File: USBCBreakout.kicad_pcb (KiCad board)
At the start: 2 copper layers, 38 x 36 mm, 8 parts, among them J1 Conn_01x04, U1 PRTR5V0U2X-ai03-locallib

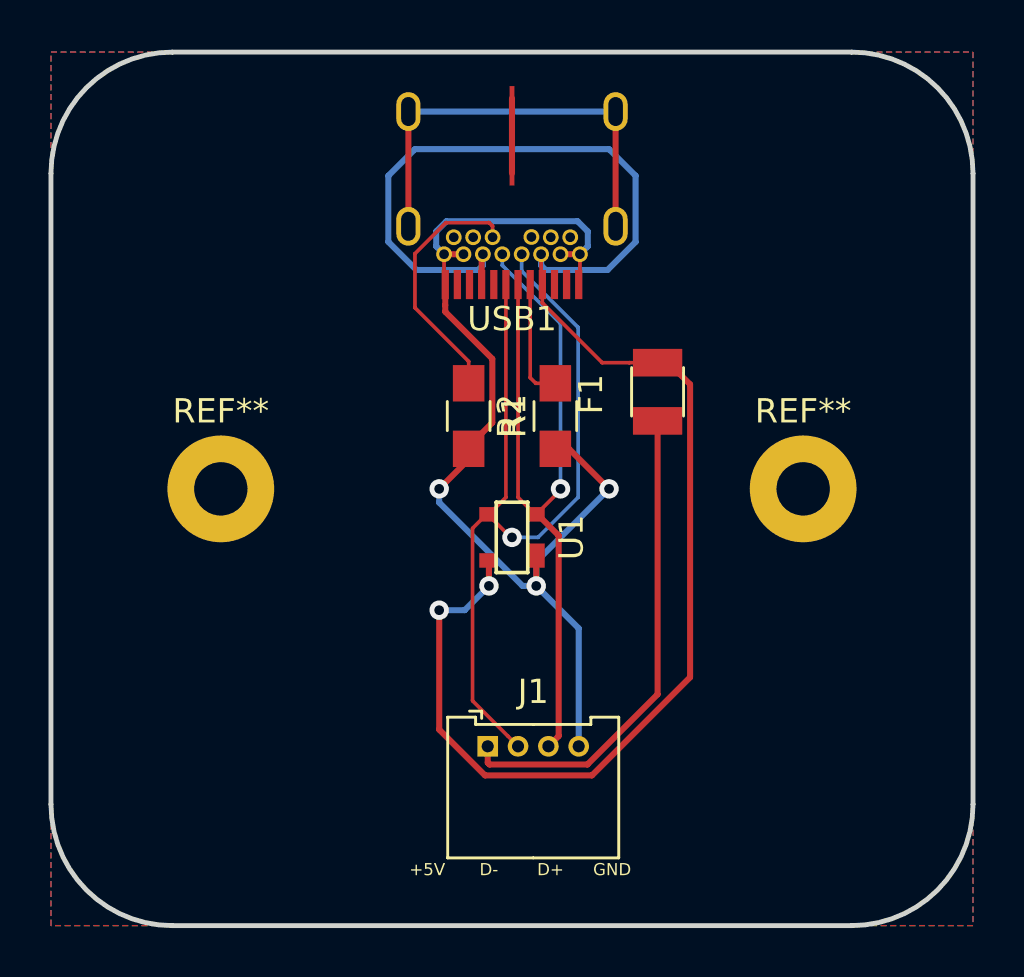
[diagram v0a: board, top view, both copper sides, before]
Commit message: Made breakout slimmer, should accomodate much better panelling.
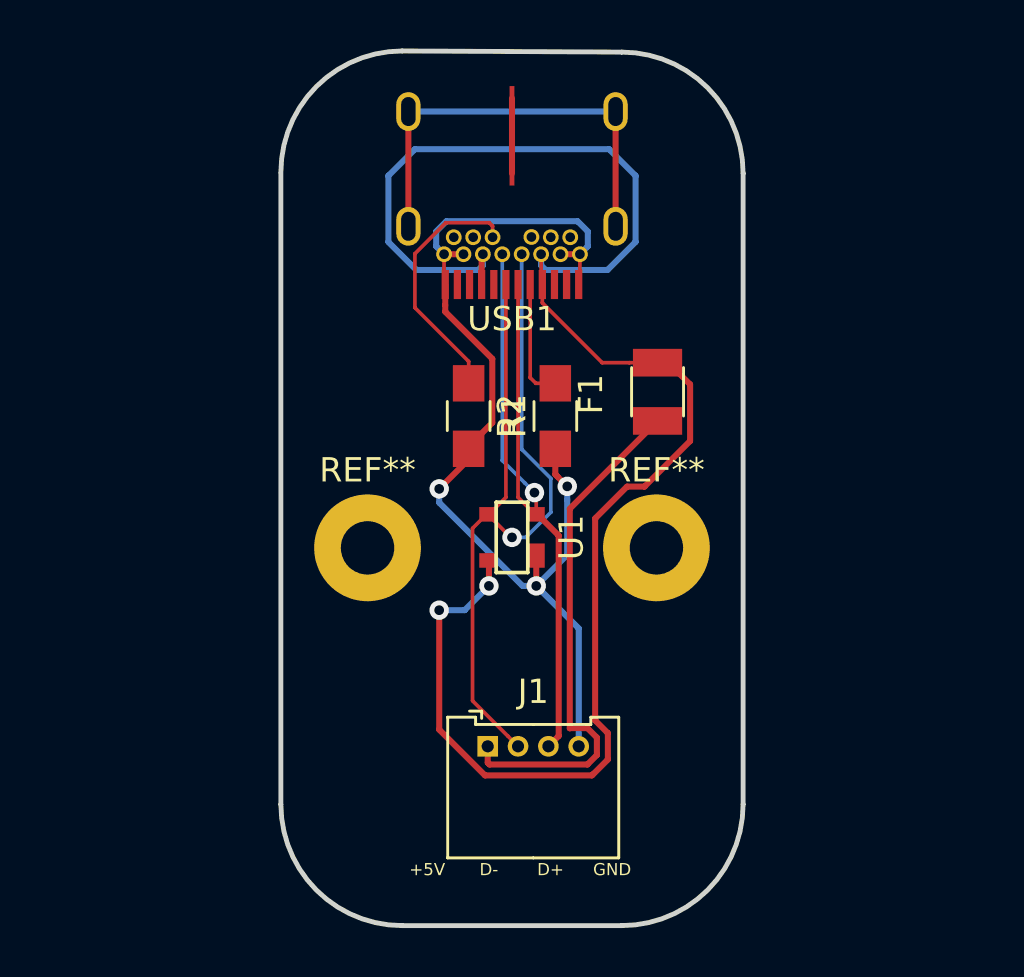
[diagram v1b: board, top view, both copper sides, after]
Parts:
- moved REF** 6.52 mm to (106.0, 60.7)
- moved REF** 6.52 mm to (94.1, 60.7)
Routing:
- net GND: track 45.7 -> 44.0 mm
- net +5V: track 20.2 -> 21.5 mm
- net D-: track 36.1 -> 34.9 mm
- net VCC: track 70.5 -> 71.3 mm
- net D+: track 32.1 -> 31.3 mm
- removed copper zone on B.Cu, net GND
- removed copper zone on F.Cu, net GND
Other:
- board size 38 x 36 mm -> 19.1 x 36 mm
